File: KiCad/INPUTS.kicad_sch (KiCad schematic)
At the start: 8 parts

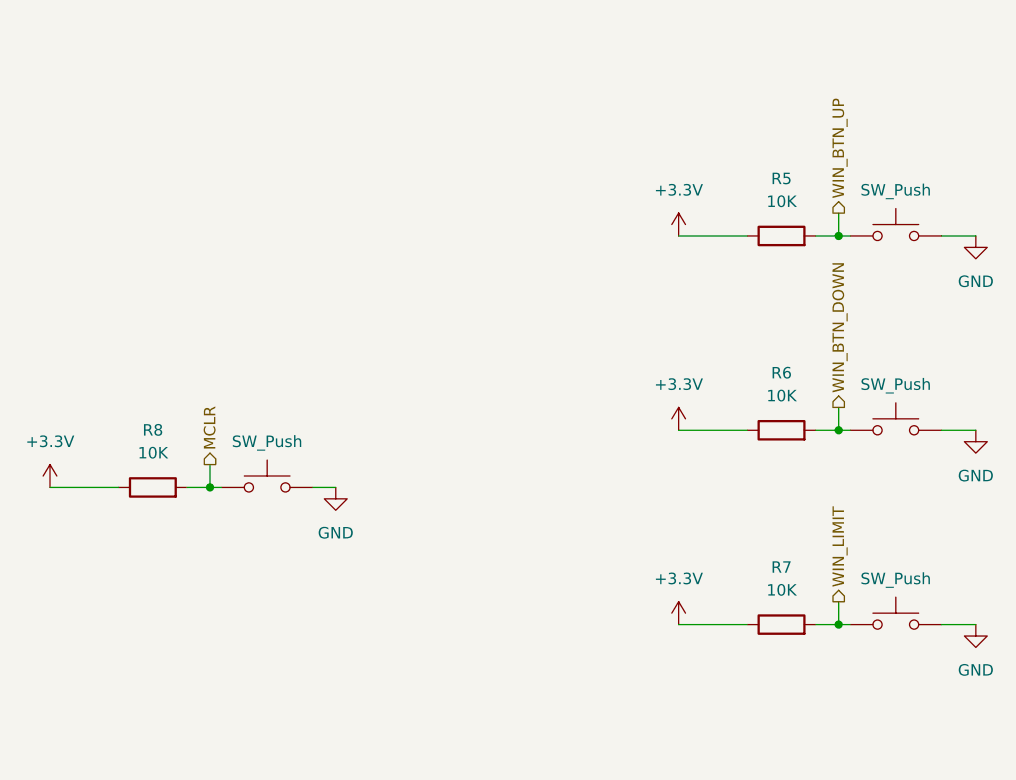
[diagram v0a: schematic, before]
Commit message: Correció etapa d'alimentació e Inputs
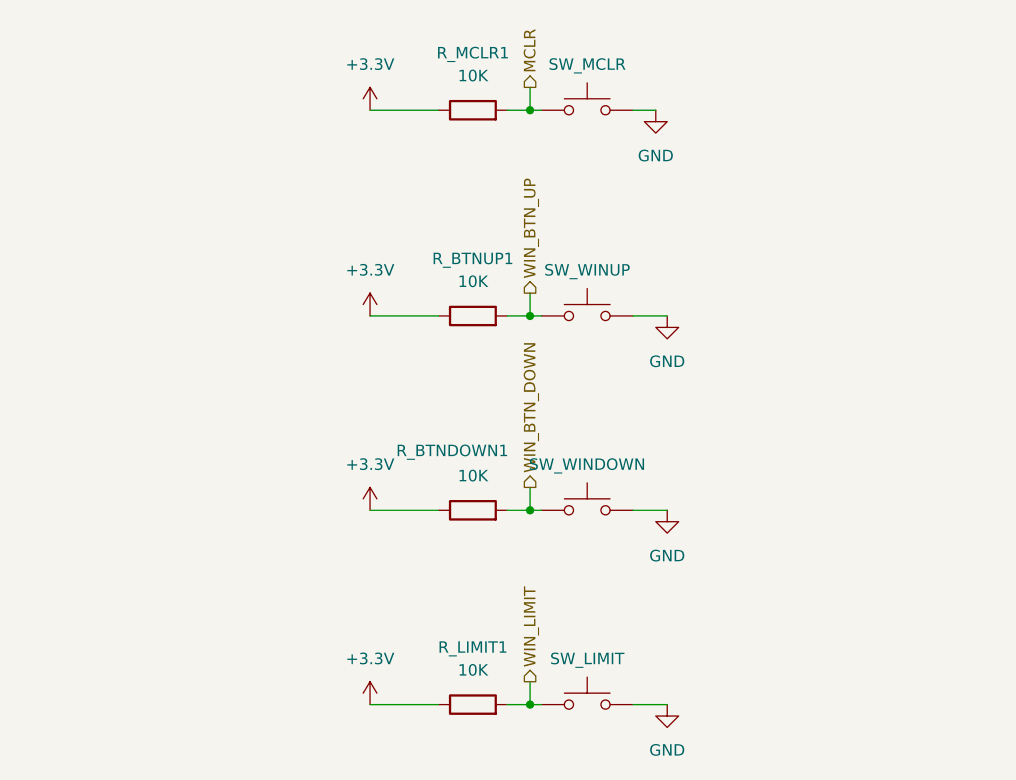
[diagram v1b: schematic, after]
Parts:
- SW_UP1: renamed from SW_UP3; value SW_Push -> SW_MCLR
- SW_UP2: renamed from SW_UP4; value SW_Push -> SW_WINUP
- SW_UP3: renamed from SW_UP1; value SW_Push -> SW_WINDOWN
- SW_UP4: renamed from SW_UP2; value SW_Push -> SW_LIMIT
- renumbered R6 to R_BTNDOWN1, R5 to R_BTNUP1, R7 to R_LIMIT1, R8 to R_MCLR1
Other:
- moved on the sheet: R_BTNDOWN1, R_BTNUP1, R_LIMIT1, R_MCLR1

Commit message: Actualizació Footprints
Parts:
- R_BTNDOWN1, R_BTNUP1, R_LIMIT1, R_MCLR1: footprint (none) -> Resistor_SMD:R_0805_2012Metric
- SW_UP1, SW_UP2, SW_UP3, SW_UP4: footprint (none) -> Button_Switch_SMD:SW_SPST_TL3342
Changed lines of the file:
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@@
 			)
 		)
-		(property "Footprint" ""
+		(property "Footprint" "Resistor_SMD:R_0805_2012Metric"
 			(at 139.7 74.168 90)
 			(effects
@@
 			)
 		)
-		(property "Footprint" ""
+		(property "Footprint" "Resistor_SMD:R_0805_2012Metric"
 			(at 139.7 95.758 90)
 			(effects
@@
 			)
 		)
-		(property "Footprint" ""
+		(property "Footprint" "Button_Switch_SMD:SW_SPST_TL3342"
 			(at 152.4 67.31 0)
 			(effects
@@
 			)
 		)
-		(property "Footprint" ""
+		(property "Footprint" "Resistor_SMD:R_0805_2012Metric"
 			(at 139.7 117.348 90)
 			(effects
@@
 			)
 		)
-		(property "Footprint" ""
+		(property "Footprint" "Resistor_SMD:R_0805_2012Metric"
 			(at 139.7 51.308 90)
 			(effects
@@
 			)
 		)
-		(property "Footprint" ""
+		(property "Footprint" "Button_Switch_SMD:SW_SPST_TL3342"
 			(at 152.4 88.9 0)
 			(effects
@@
 			)
 		)
-		(property "Footprint" ""
+		(property "Footprint" "Button_Switch_SMD:SW_SPST_TL3342"
 			(at 152.4 110.49 0)
 			(effects
@@
 			)
 		)
-		(property "Footprint" ""
+		(property "Footprint" "Button_Switch_SMD:SW_SPST_TL3342"
 			(at 152.4 44.45 0)
 			(effects

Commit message: Versió final Esquematic
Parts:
- added R_BTNDOWN2, R_BTNUP2, R_LOCK1, R_UNLOCK1: 10K, Resistor_SMD:R_0805_2012Metric, symbol Device:R
- added SW_UP5: SW_WINUP, Button_Switch_SMD:SW_SPST_TL3342, symbol Switch:SW_Push
- added SW_UP6: SW_WINDOWN, Button_Switch_SMD:SW_SPST_TL3342, symbol Switch:SW_Push
- added SW_UP7, SW_UP8: SW_LIMIT, Button_Switch_SMD:SW_SPST_TL3342, symbol Switch:SW_Push
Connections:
- net +3.3V: now also R_BTNDOWN2.1, R_BTNUP2.1, R_LOCK1.1, R_UNLOCK1.1
- net GND: now also SW_UP5.2, SW_UP6.2, SW_UP7.2, SW_UP8.2
- new net DOOR_BTN_CLOSED: R_BTNDOWN2.2, SW_UP6.1
- new net DOOR_BTN_OPEN: R_BTNUP2.2, SW_UP5.1
- new net DOOR_LOCK_SW: R_LOCK1.2, SW_UP7.1
- new net DOOR_UNLOCK_SW: R_UNLOCK1.2, SW_UP8.1
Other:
- moved on the sheet: R_BTNDOWN1, R_BTNUP1, R_LIMIT1, R_MCLR1

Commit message: Versió final de l'esquematic
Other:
- note added: "BOTONERA DE LA FINESTRA"
- note added: "BOTONERA DE LA PORTA"
- note added: "MCLR"
- moved on the sheet: R_BTNDOWN1, R_BTNDOWN2, R_BTNUP1, R_BTNUP2, R_LIMIT1, R_LOCK1, R_MCLR1, R_UNLOCK1

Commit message: 1ra versióPCB
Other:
- moved on the sheet: R_MCLR1
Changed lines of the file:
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@@
 	(text "MCLR"
 		(exclude_from_sim no)
-		(at 40.64 24.384 0)
+		(at 38.1 24.384 0)
 		(effects
 			(font
@@
 	)
 	(junction
-		(at 45.72 44.45)
+		(at 43.18 44.45)
 		(diameter 0)
 		(color 0 0 0 0)
@@
 	(wire
 		(pts
-			(xy 57.15 44.45) (xy 59.69 44.45)
-		)
-		(stroke
-			(width 0)
-			(type default)
-		)
-	)
-	(wire
-		(pts
-			(xy 43.18 44.45) (xy 45.72 44.45)
+			(xy 54.61 44.45) (xy 57.15 44.45)
+		)
+		(stroke
+			(width 0)
+			(type default)
+		)
+	)
+	(wire
+		(pts
+			(xy 40.64 44.45) (xy 43.18 44.45)
 		)
 		(stroke
@@
 	(wire
 		(pts
-			(xy 45.72 41.91) (xy 45.72 44.45)
+			(xy 43.18 41.91) (xy 43.18 44.45)
 		)
 		(stroke
@@
 	(wire
 		(pts
-			(xy 27.94 44.45) (xy 35.56 44.45)
+			(xy 25.4 44.45) (xy 33.02 44.45)
 		)
 		(stroke
@@
 	(wire
 		(pts
-			(xy 45.72 44.45) (xy 46.99 44.45)
+			(xy 43.18 44.45) (xy 44.45 44.45)
 		)
 		(stroke
@@
 	(hierarchical_label "MCLR"
 		(shape output)
-		(at 45.72 41.91 90)
+		(at 43.18 41.91 90)
 		(effects
 			(font
@@
 	(symbol
 		(lib_id "power:+3.3V")
-		(at 27.94 44.45 0)
+		(at 25.4 44.45 0)
 		(unit 1)
 		(exclude_from_sim no)
@@
 		(fields_autoplaced yes)
 		(property "Reference" "#PWR022"
-			(at 27.94 48.26 0)
+			(at 25.4 48.26 0)
 			(effects
 				(font
@@
 		)
 		(property "Value" "+3.3V"
-			(at 27.94 39.37 0)
+			(at 25.4 39.37 0)
 			(effects
 				(font
@@
 		)
 		(property "Footprint" ""
-			(at 27.94 44.45 0)
+			(at 25.4 44.45 0)
 			(effects
 				(font
@@
 		)
 		(property "Datasheet" ""
-			(at 27.94 44.45 0)
+			(at 25.4 44.45 0)
 			(effects
 				(font
@@
 		)
 		(property "Description" "Power symbol creates a global label with name \"+3.3V\""
-			(at 27.94 44.45 0)
+			(at 25.4 44.45 0)
 			(effects
 				(font
@@
 	(symbol
 		(lib_id "Device:R")
-		(at 39.37 44.45 90)
+		(at 36.83 44.45 90)
 		(unit 1)
 		(exclude_from_sim no)
@@
 		(fields_autoplaced yes)
 		(property "Reference" "R_MCLR1"
-			(at 39.37 38.1 90)
+			(at 36.83 38.1 90)
 			(effects
 				(font
@@
 		)
 		(property "Value" "10K"
-			(at 39.37 40.64 90)
+			(at 36.83 40.64 90)
 			(effects
 				(font
@@
 		)
 		(property "Footprint" "Resistor_SMD:R_0805_2012Metric"
-			(at 39.37 46.228 90)
+			(at 36.83 46.228 90)
 			(effects
 				(font
@@
 		)
 		(property "Datasheet" "~"
-			(at 39.37 44.45 0)
+			(at 36.83 44.45 0)
 			(effects
 				(font
@@
 		)
 		(property "Description" "Resistor"
-			(at 39.37 44.45 0)
+			(at 36.83 44.45 0)
 			(effects
 				(font
@@
 	(symbol
 		(lib_id "Switch:SW_Push")
-		(at 52.07 44.45 0)
+		(at 49.53 44.45 0)
 		(unit 1)
 		(exclude_from_sim no)
@@
 		(fields_autoplaced yes)
 		(property "Reference" "SW_UP1"
-			(at 52.07 36.83 0)
+			(at 49.53 36.83 0)
 			(effects
 				(font
@@
 		)
 		(property "Value" "SW_MCLR"
-			(at 52.07 39.37 0)
+			(at 49.53 39.37 0)
 			(effects
 				(font
@@
 		)
 		(property "Footprint" "Button_Switch_SMD:SW_SPST_TL3342"
-			(at 52.07 39.37 0)
+			(at 49.53 39.37 0)
 			(effects
 				(font
@@
 		)
 		(property "Datasheet" "~"
-			(at 52.07 39.37 0)
+			(at 49.53 39.37 0)
 			(effects
 				(font
@@
 		)
 		(property "Description" "Push button switch, generic, two pins"
-			(at 52.07 44.45 0)
+			(at 49.53 44.45 0)
 			(effects
 				(font
@@
 	(symbol
 		(lib_id "power:GND")
-		(at 59.69 44.45 0)
+		(at 57.15 44.45 0)
 		(unit 1)
 		(exclude_from_sim no)
@@
 		(fields_autoplaced yes)
 		(property "Reference" "#PWR023"
-			(at 59.69 50.8 0)
+			(at 57.15 50.8 0)
 			(effects
 				(font
@@
 		)
 		(property "Value" "GND"
-			(at 59.69 49.53 0)
+			(at 57.15 49.53 0)
 			(effects
 				(font
@@
 		)
 		(property "Footprint" ""
-			(at 59.69 44.45 0)
+			(at 57.15 44.45 0)
 			(effects
 				(font
@@
 		)
 		(property "Datasheet" ""
-			(at 59.69 44.45 0)
+			(at 57.15 44.45 0)
 			(effects
 				(font
@@
 		)
 		(property "Description" "Power symbol creates a global label with name \"GND\" , ground"
-			(at 59.69 44.45 0)
-			(effects
-				(font
+			(at 57.15 44.45 0)
+			(effects
+				(font

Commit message: Inputs
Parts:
- removed R_BTNDOWN2, R_BTNUP2, R_LOCK1: 10K, Resistor_SMD:R_0805_2012Metric, symbol Device:R
- removed SW_UP2, SW_UP5: SW_WINUP, Button_Switch_SMD:SW_SPST_TL3342, symbol Switch:SW_Push
- removed SW_UP3, SW_UP6: SW_WINDOWN, Button_Switch_SMD:SW_SPST_TL3342, symbol Switch:SW_Push
- removed SW_UP7, SW_UP8: SW_LIMIT, Button_Switch_SMD:SW_SPST_TL3342, symbol Switch:SW_Push
- added SW3: SW_SPDT_MSM, Button_Switch_SMD:SW_DPDT_CK_JS202011JCQN, symbol Switch:SW_SPDT_MSM
- added SW4: SW_DPDT_x2, Button_Switch_THT:SW_CK_JS202011CQN_DPDT_Straight, symbol Switch:SW_DPDT_x2
- renumbered R_UNLOCK1 to R_Lock/Unlock
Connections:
- net +3.3V: now also SW4.1 (A); no longer R_BTNDOWN1.1, R_BTNUP1.1, R_Lock/Unlock.1
- net GND: now also R_BTNDOWN1.2, R_BTNUP1.2, SW3.2 (3), SW4.3 (C)
- net WIN_BTN_DOWN: now also R_BTNDOWN1.1, SW3.3 (4); no longer R_BTNDOWN1.2
- net WIN_BTN_UP: now also R_BTNUP1.1, SW3.1; no longer R_BTNUP1.2
- net DOOR_UNLOCK_SW: no longer names the net of R_Lock/Unlock.2
- net DOOR_UNLOCK_SW: now also SW4.2 (B)
- new net DOOR_LOCK/UNLOCK: R_Lock/Unlock.1
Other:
- note added: "0 lògic - Desbloqueig"
- note added: "1 lògic - Bloqueig"
- moved on the sheet: R_BTNDOWN1, R_BTNUP1, R_LIMIT1, R_Lock/Unlock, R_MCLR1

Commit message: Actulitació de components
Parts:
- renumbered R_Lock/Unlock to R_Lock/Unlock1
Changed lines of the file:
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@@
 		(on_board yes)
 		(dnp no)
-		(property "Reference" "R_Lock/Unlock"
+		(property "Reference" "R_Lock/Unlock1"
 			(at 164.084 35.306 90)
 			(effects
@@
 			(project "PROJECTE_EINES"
 				(path "/347831db-5db9-4aff-ad32-e56fd770e219/85b10b44-f8b7-4b58-879f-bd15e6c8e976"
-					(reference "R_Lock/Unlock")
+					(reference "R_Lock/Unlock1")
 					(unit 1)
 				)
